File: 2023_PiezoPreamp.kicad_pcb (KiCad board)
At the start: 4 copper layers, 70 x 35.5 mm, 73 parts, among them J101 6.3mm stereo, J102 6.3mm stereo, J201 Molex PicoBlade, J301 2.54mm header, J401 Spring Contact, U101 OPA145, U102 OPA145, U201 ZXMP3A17E6TA, U301 MMDT2222A-7-F

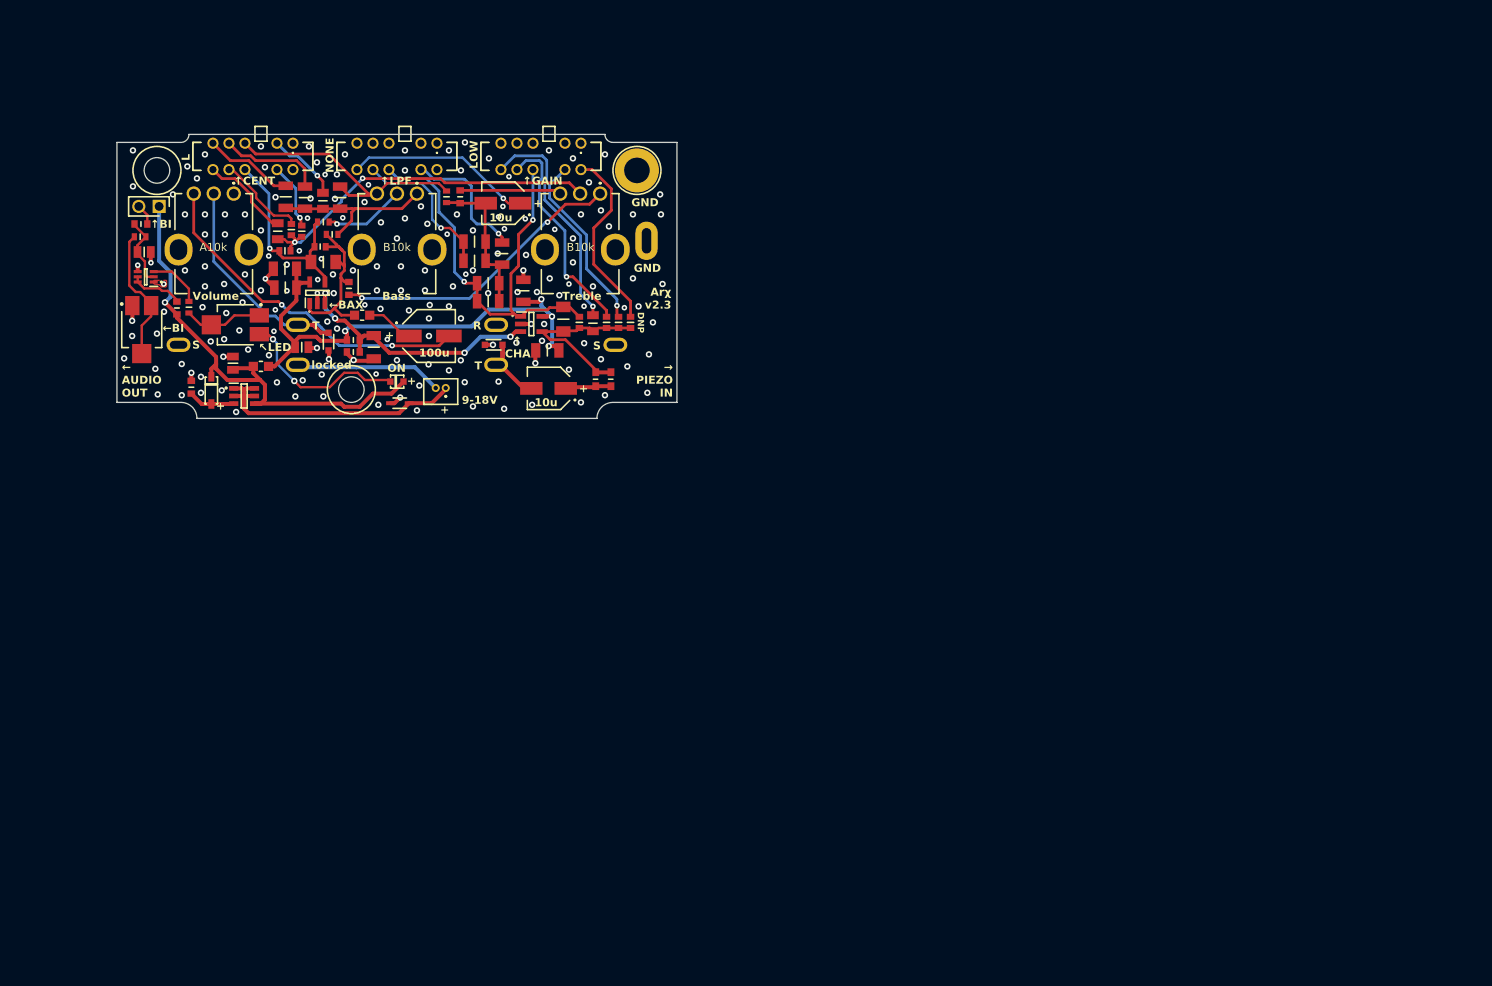
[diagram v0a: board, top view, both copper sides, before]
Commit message: improving the schematic - v3.0. Very crude draft of board layout with battery holder underneath the PCB
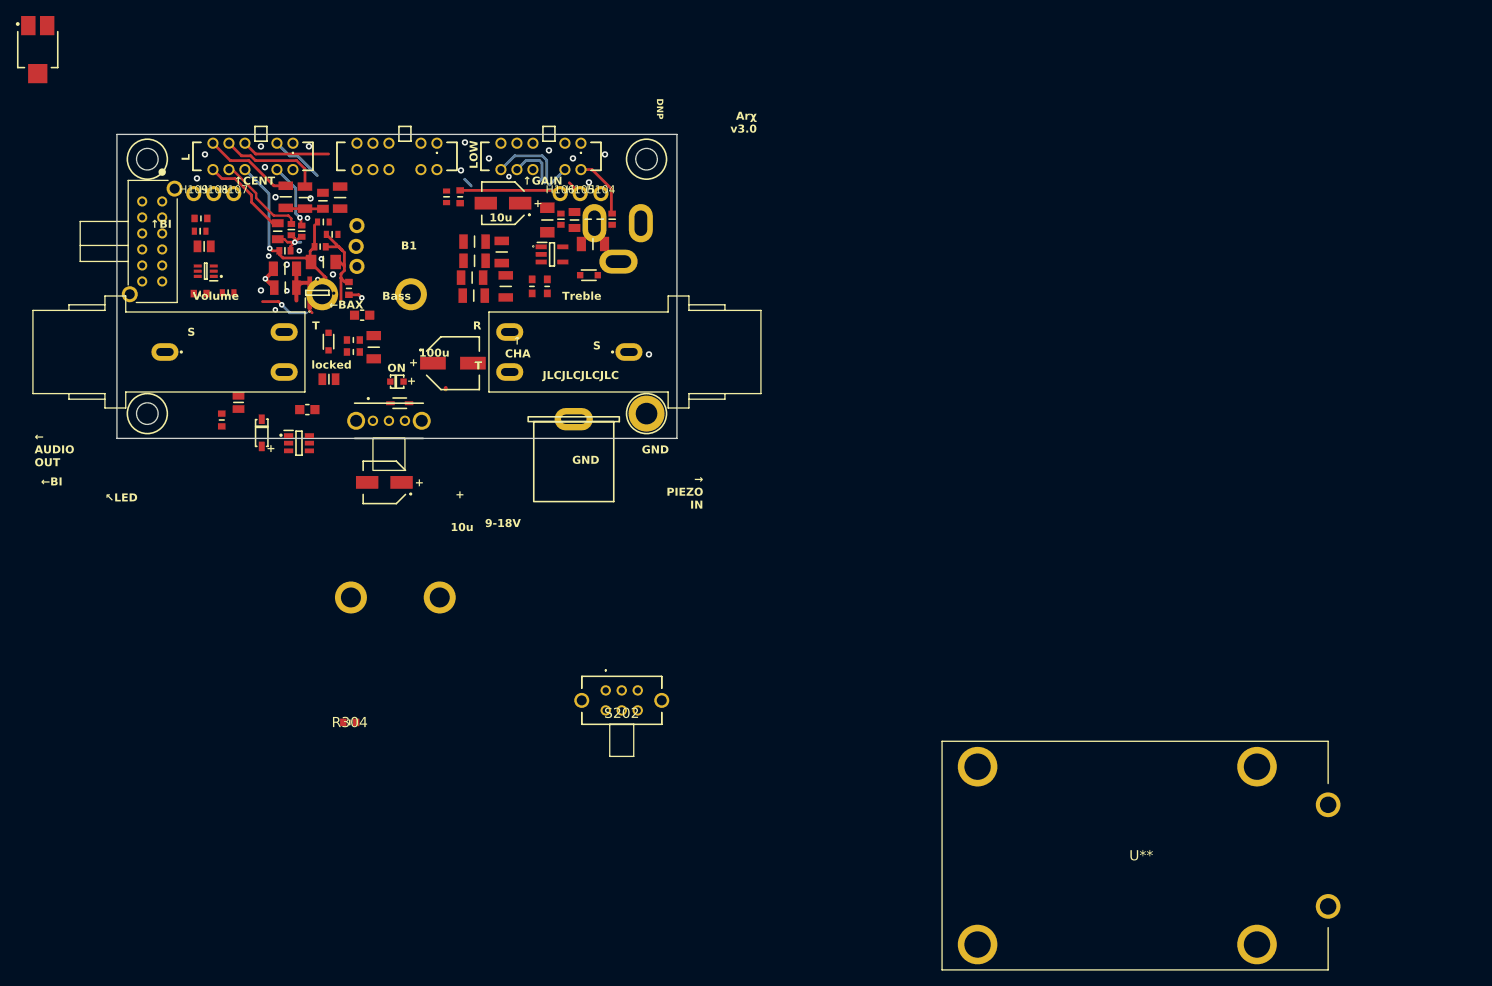
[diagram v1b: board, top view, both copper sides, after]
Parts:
- removed J301: 2.54mm header, library:77311-818-02
- removed RV101, RV102: B10k, library:PTV09A-4020F-A103
- removed RV103: A10k, library:PTV09A-4020F-A103
- removed RV302: trim B10k, library:ST-4ETB103
- added H101: Bass 1, library:FreePad_1.1mm_2.0mm, F.Cu at (69.0, 40.9)
- added H102: Bass 2, library:FreePad_1.1mm_2.0mm, F.Cu at (68.9, 43.5)
- added H103: Bass 3, library:FreePad_1.1mm_2.0mm, F.Cu at (69.0, 46.0)
- added H104: Treble 1, library:FreePad_1.1mm_2.0mm, F.Cu at (99.5, 36.9)
- added H105: Treble 2, library:FreePad_1.1mm_2.0mm, F.Cu at (96.9, 36.9)
- added H106: Treble 3, library:FreePad_1.1mm_2.0mm, F.Cu at (94.4, 36.9)
- added H107: Volume 1, library:FreePad_1.1mm_2.0mm, F.Cu at (53.6, 36.9)
- added H108: Volume 2, library:FreePad_1.1mm_2.0mm, F.Cu at (51.1, 36.9)
- added H109: Volume 3, library:FreePad_1.1mm_2.0mm, F.Cu at (48.6, 36.9)
- added H402: M2.5 MountingHole, MountingHole:MountingHole_2.7mm_M2.5_ISO14580, F.Cu at (42.8, 64.4)
- added H414: 9V battery holder, library:KEYSTONE-71, B.Cu at (73.8, 87.4)
- added H414: 9V battery holder, library:KEYSTONE-71, B.Cu at (70.2, 49.5)
- added R304: 10k, library:RT0603BRD0710KL, F.Cu at (68.1, 103.0)
- added REF**: Volume, library:pot_R16148-1A-1_FabOnly, F.Cu at (54.9, 42.8)
- added REF**: Bass, library:pot_R16148-1A-1_FabOnly, F.Cu at (74.0, 42.8)
- added REF**: Treble, library:pot_R16148-1A-1_FabOnly, F.Cu at (93.1, 42.8)
- added S201: EG4208A, library:EG4208A, F.Cu at (43.4, 42.9)
- added S202: EG2208, library:EG2208, F.Cu at (100.1, 99.0)
- added S301: OS102011MA1QN1, library:OS102011MA1QN1, F.Cu at (73.0, 65.3)
- added U**: 129179, library:1291-79, F.Cu at (190.4, 126.0)
- H401: value M3 MountingHole_Pad -> M2.5 MountingHole_Pad; footprint MountingHole:MountingHole_3.2mm_M3_ISO14580_Pad -> MountingHole:MountingHole_2.7mm_M2.5_ISO14580_Pad
- H403: renamed from H402; value M3 MountingHole -> M2.5 MountingHole; footprint MountingHole:MountingHole_3.2mm_M3_ISO14580 -> MountingHole:MountingHole_2.7mm_M2.5_ISO14580
- H404: renamed from H403; value M3 MountingHole -> M2.5 MountingHole; footprint MountingHole:MountingHole_3.2mm_M3_ISO14580 -> MountingHole:MountingHole_2.7mm_M2.5_ISO14580
- J101, J102, J401: moved to F.Cu
- J201: value Molex PicoBlade -> DC IN 5.5/2.1mm; footprint library:53047-0210 -> library:694106301002; moved to B.Cu
- moved H404 46.8 mm to (105.2, 32.6)
- moved RV301 37.3 mm to (29.1, 18.9)
- moved J201 36.3 mm to (112.3, 44.4), turned to 180 degrees
- moved H401 30.4 mm to (105.2, 64.4)
- moved J401 24.1 mm to (96.1, 65.1), turned to 180 degrees
- moved C101 23.7 mm to (72.4, 73.0)
- moved D101 14.7 mm to (98.0, 47.1)
- moved C205 14.5 mm to (98.5, 43.2)
- moved R102 14.1 mm to (92.8, 48.5)
- moved R101 14.1 mm to (90.9, 48.5)
- moved Cf101 13.1 mm to (94.5, 40.1)
- moved Cf102 13.1 mm to (96.2, 40.2)
- moved Cf103 13.1 mm to (97.9, 40.1)
- moved Cf104 13.1 mm to (99.4, 40.1)
- moved Cf105 13.1 mm to (100.9, 40.1)
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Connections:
- C101 pad 2: /1-ChargeAmpAndEQ/PIEZO_IN -> PIEZO_ESD
- D101 pad 2: /1-ChargeAmpAndEQ/PIEZO_IN -> PIEZO_ESD
- D102 pad 2: /1-ChargeAmpAndEQ/AUDIO_OUT -> AUDIO_ESD
- D201 pad 2: /2-Power/DC_IN_POS -> /2-Power/DC_IN_ESD
- J101 pad 2: /1-ChargeAmpAndEQ/PIEZO_IN -> PIEZO_IN
- J102 pad 2: /1-ChargeAmpAndEQ/AUDIO_OUT -> AUDIO_OUT
- J201 pad 1: /2-Power/DC_IN_POS -> DC_IN_NEG
- J201 pad 2: DC_IN_NEG -> /2-Power/DC_IN_POS
- U201 pad 1: /2-Power/DC_IN_POS -> /2-Power/DC_IN_ESD
- U201 pad 2: /2-Power/DC_IN_POS -> /2-Power/DC_IN_ESD
- U201 pad 5: /2-Power/DC_IN_POS -> /2-Power/DC_IN_ESD
- U201 pad 6: /2-Power/DC_IN_POS -> /2-Power/DC_IN_ESD
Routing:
- net Vbi: track 60.8 -> 0.00 mm, vias 1 -> 0
- net VS: track 65.8 -> 5.98 mm, vias 4 -> 0
- net /1-ChargeAmpAndEQ/CH_A_OUT: track 58.3 -> 0.00 mm, vias 2 -> 0
- net /1-ChargeAmpAndEQ/TR_2: track 45.7 -> 8.45 mm, vias 2 -> 1
- net /1-ChargeAmpAndEQ/VOL_3: track 43.2 -> 6.08 mm, vias 2 -> 1
- net /1-ChargeAmpAndEQ/TR_1: track 37.0 -> 1.87 mm, vias 2 -> 1
- net /2-Power/DC_IN_POS: track 35.7 -> 1.20 mm
- net Vbias: track 33.6 -> 1.22 mm, vias 4 -> 1
- net /1-ChargeAmpAndEQ/AUDIO_OUT: track 26.5 -> 0.00 mm
- net /1-ChargeAmpAndEQ/LPF_SW_6: track 23.4 -> 0.00 mm, vias 1 -> 0
- net /1-ChargeAmpAndEQ/BA_3: track 33.9 -> 11.0 mm
- net /1-ChargeAmpAndEQ/CH_A_INV: track 22.5 -> 0.00 mm
- net /3-BatteryIndicator/LED_K: track 21.7 -> 0.00 mm, vias 2 -> 0
- net /1-ChargeAmpAndEQ/G_SW_7: track 27.0 -> 6.17 mm, vias 1 -> 0
- net /1-ChargeAmpAndEQ/G_SW_9: track 22.9 -> 2.72 mm, vias 1 -> 0
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- removed copper zone on F.Cu, net GND
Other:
- board size 70 x 35.5 mm -> 70 x 38 mm
- board text added: "Arχ v3.0"
- board text added: "B1"
- board text added: "Piezo Preamp + EQ v3.0 02/2024 Arχ arx.wtf"
- board text added: "board outline tolerane: 0.2mm on every side"
- board text added: "washer"
- board text removed: "Arχ v2.3"
- board text removed: "B"
- board text removed: "NONE"
- board text removed: "Piezo Preamp + EQ v2.3 01/2024 Arχ arx.wtf"
- board text removed: "↑LPF"

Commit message: working on component placement, improving schematics
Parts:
- removed the H414 at (73.8, 87.4)
- removed S202: EG2208, library:EG2208
- removed U**: 129179, library:1291-79
- added C**: B32529C105J, library:cap_B32529C105J, F.Cu at (197.6, 84.8)
- C101: value 10u 50V -> 0.47u; footprint library:EEEFK1H100UR -> library:GRM31C5C1E474JE01L
- S301: moved to B.Cu
- moved R202 154.0 mm to (207.3, 117.2)
- moved C201 150.8 mm to (194.6, 118.0)
- moved R201 149.6 mm to (192.0, 118.2)
- moved D202 149.5 mm to (197.3, 118.7)
- moved U201 149.3 mm to (202.5, 118.0)
- moved Volume 121.4 mm to (176.1, 50.5)
- moved RV301 118.7 mm to (127.1, 85.8)
- moved S201 108.1 mm to (130.3, 107.2), turned to 0 degrees
- moved C101 102.2 mm to (172.4, 94.0), turned to 0 degrees
- moved H109 96.0 mm to (127.0, 92.3)
- moved H108 95.9 mm to (129.4, 92.2)
- moved R104 92.4 mm to (146.4, 88.8)
- moved Rt102 92.1 mm to (147.8, 94.8), turned to 180 degrees
- moved H107 90.1 mm to (124.6, 92.3)
- moved J201 89.4 mm to (189.2, 90.0)
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- renumbered REF** to Bass, REF** to Treble, REF** to Volume
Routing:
- net /1-ChargeAmpAndEQ/BAX_A_INV: track 25.4 -> 0.00 mm, vias 1 -> 0
- net /1-ChargeAmpAndEQ/BAX_A_OUT: track 15.9 -> 0.00 mm
- net /1-ChargeAmpAndEQ/C_SW_4: track 13.0 -> 0.00 mm
- net /1-ChargeAmpAndEQ/TR_3: track 12.7 -> 0.00 mm
- net /1-ChargeAmpAndEQ/C_SW_6: track 11.4 -> 0.00 mm
- net /1-ChargeAmpAndEQ/C_SW_7: track 11.4 -> 0.00 mm
- net /1-ChargeAmpAndEQ/C_SW_5: track 11.3 -> 0.00 mm
- net /1-ChargeAmpAndEQ/BA_3: track 11.0 -> 0.00 mm
- net /1-ChargeAmpAndEQ/G_SW_6: track 9.87 -> 0.00 mm
- net /1-ChargeAmpAndEQ/TR_2: track 8.45 -> 0.00 mm, vias 1 -> 0
- net /1-ChargeAmpAndEQ/C_SW_9: track 8.28 -> 0.00 mm, vias 1 -> 0
- net /1-ChargeAmpAndEQ/G_SW_10: track 7.49 -> 0.00 mm
- net /1-ChargeAmpAndEQ/C_SW_2: track 6.73 -> 0.00 mm
- net /1-ChargeAmpAndEQ/G_SW_7: track 6.17 -> 0.00 mm
- net /1-ChargeAmpAndEQ/VOL_3: track 6.08 -> 0.00 mm, vias 1 -> 0
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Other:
- board size 70 x 38 mm -> 71 x 38 mm
- board text added: "Bass pot (tight) X = 35.5, Y = 9.8"
- board text added: "Treble pot (tight) X = 12.6, Y = 9.8"
- board text added: "Volume pot (loose) X = 60+, Y = 12.3"

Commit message: saving PCB in kicad 8 format
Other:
- board text removed: "locked"

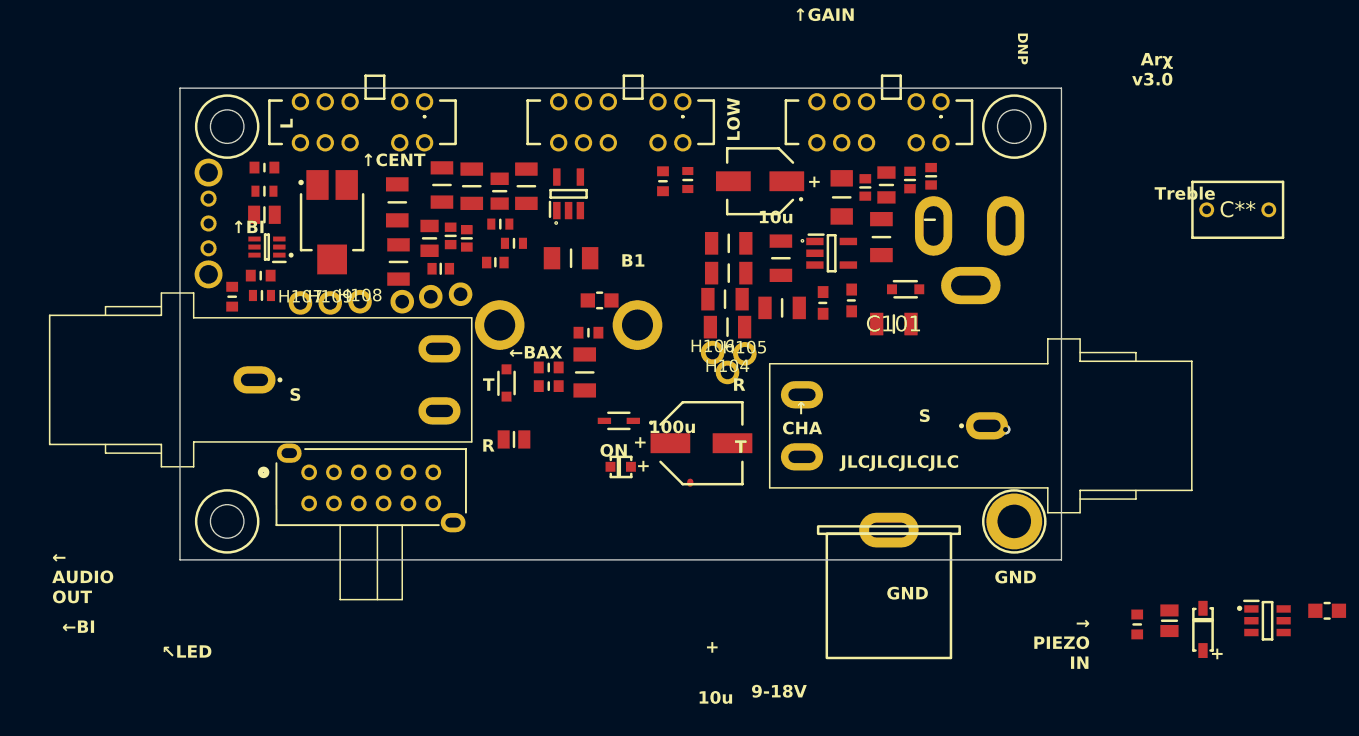
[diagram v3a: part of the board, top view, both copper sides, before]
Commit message: PCB: updating footprints from schematic
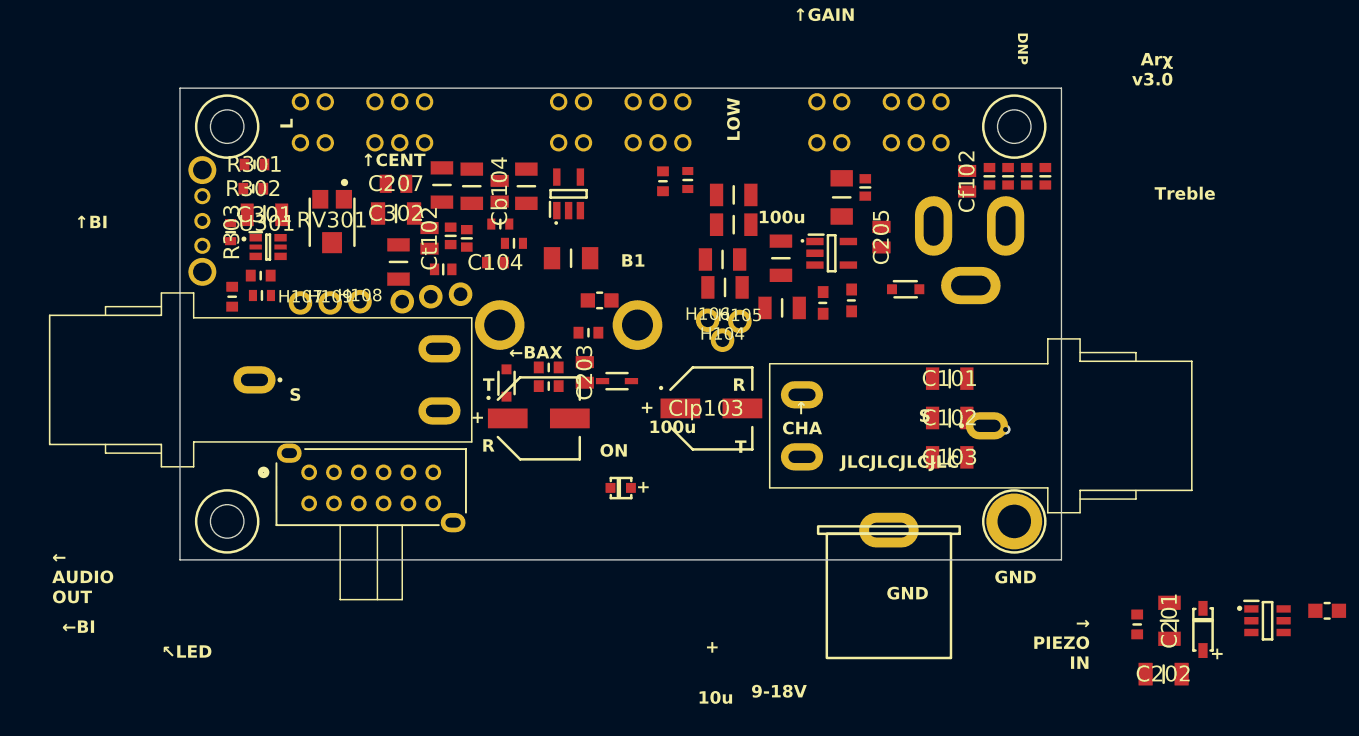
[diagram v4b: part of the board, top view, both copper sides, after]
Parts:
- removed C**: B32529C105J, library:cap_B32529C105J
- added C102: 220n, library:GRM31C5C1H224JE02L, F.Cu at (176.9, 101.6)
- added C103: 220n, library:GRM31C5C1H224JE02L, F.Cu at (176.9, 104.8)
- added C302: 22u, library:cap_CL31A226KAHNNNE, F.Cu at (132.3, 85.2)
- added Cf104: 4n7, library:GRM1885C1H472JA01D, F.Cu at (180.1, 82.2)
- added R303: 3k9, library:ERA-3AEB392V, F.Cu at (119.0, 86.7)
- C101: value 0.47u -> 220n; footprint library:GRM31C5C1E474JE01L -> library:GRM31C5C1H224JE02L
- C104: renamed from C102; footprint library:GRM1885C1H101JA01D -> library:cap_CL10C101JB8NNNC
- C201, C202, C301: footprint library:GRM21BR61E226ME44L -> library:cap_CL31A226KAHNNNE
- C203, C205, C207: footprint library:C3216X5R1H106K160AB -> library:cap_CL21A106KAYNNNE
- Cb104, Cf102, Ct102: footprint library:CGA4J2C0G1H223J125AA -> library:GRM21B5C1H223JA01L
- Cf103: value 10n -> 4n7; footprint library:GRM1885C1H103JA01D -> library:GRM1885C1H472JA01D
- Clp103: value 10u 50V -> 100u 50V; footprint library:EEEFK1H100UR -> library:EEEFTH101XAP
- R301: value 100k -> 47k; footprint library:RT0603BRD07100KL -> library:RT0603BRD0747KL
- R302: value 3k9 -> 47k; footprint library:ERA-3AEB392V -> library:RT0603BRD0747KL
- RV301: footprint library:ST-4ETB103 -> library:trimpot_TC33X-2-103E
- S101, S102, S103: moved to B.Cu
- U301: value MMDT2222A-7-F -> BC847BS,115; footprint library:MMDT2222A-7-F -> library:bjt_BC847BS_115
- moved C202 55.6 mm to (194.1, 122.2)
- moved Bass 37.4 mm to (150.4, 84.8)
- moved Treble 35.4 mm to (127.5, 84.8)
- moved Volume 34.5 mm to (173.3, 84.8)
- moved Clp103 18.7 mm to (157.7, 100.8), turned to 0 degrees
- moved C105 13.3 mm to (143.8, 101.7)
- moved Cf106 9.20 mm to (184.6, 82.2)
- moved Cf105 8.55 mm to (183.1, 82.2)
- moved Cf103 7.91 mm to (181.6, 82.2)
- moved Cf102 6.51 mm to (178.3, 82.5)
- moved C101 6.29 mm to (176.9, 98.5)
- moved Clp104 3.92 mm to (159.5, 86.0)
- moved Clp105 3.92 mm to (159.5, 83.7)
- moved Clp102 3.21 mm to (158.6, 88.8)
- moved Clp101 3.21 mm to (158.8, 91.1)
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- renumbered C103 to C105, Cf104 to Cf105, Cf105 to Cf106, R303 to R304, R304 to R305
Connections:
- net Net-(S201-Pad1) renamed /2-Power/BYPASS
- C101 pad 1: /1-ChargeAmpAndEQ/CIN_RIN -> PIEZO_ESD
- C101 pad 2: PIEZO_ESD -> /1-ChargeAmpAndEQ/CIN_RIN
- C301 pad 2: /3-BatteryIndicator/BI_B2 -> /3-BatteryIndicator/BI_B1
- R301 pad 2: /3-BatteryIndicator/BI_B2 -> /3-BatteryIndicator/BI_R
- R302 pad 1: /3-BatteryIndicator/BI_B2 -> /3-BatteryIndicator/BI_R
- R302 pad 2: /3-BatteryIndicator/TRIM_BI_3 -> /3-BatteryIndicator/BI_B1
- R304 pad 2: /3-BatteryIndicator/BI_B1 -> /3-BatteryIndicator/BI_C1_B2
- R305 pad 2: /3-BatteryIndicator/BI_C1 -> /3-BatteryIndicator/BI_C2
- U301 pad 2: /3-BatteryIndicator/BI_B2 -> /3-BatteryIndicator/BI_B1
- U301 pad 3: /3-BatteryIndicator/BI_C1 -> /3-BatteryIndicator/BI_C2
- U301 pad 5: /3-BatteryIndicator/BI_B1 -> /3-BatteryIndicator/BI_C1_B2
- U301 pad 6: /3-BatteryIndicator/BI_B1 -> /3-BatteryIndicator/BI_C1_B2
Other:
- board text added: "Bass pot tight: X = 35.5, Y = 9.8 loose: X = 35.5, Y = 12.3"
- board text added: "Treble pot tight: X = 12.6, Y = 9.8 loose: X = , Y = 12.3"
- board text added: "Volume pot tight: X = 58.4, Y = 9.8 loose: X = 60+, Y = 12.3"
- board text added: "jack Y = 27.2"
- board text removed: "Bass pot (tight) X = 35.5, Y = 9.8"
- board text removed: "Treble pot (tight) X = 12.6, Y = 9.8"
- board text removed: "Volume pot (loose) X = 60+, Y = 12.3"
